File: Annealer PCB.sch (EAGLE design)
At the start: 36 parts

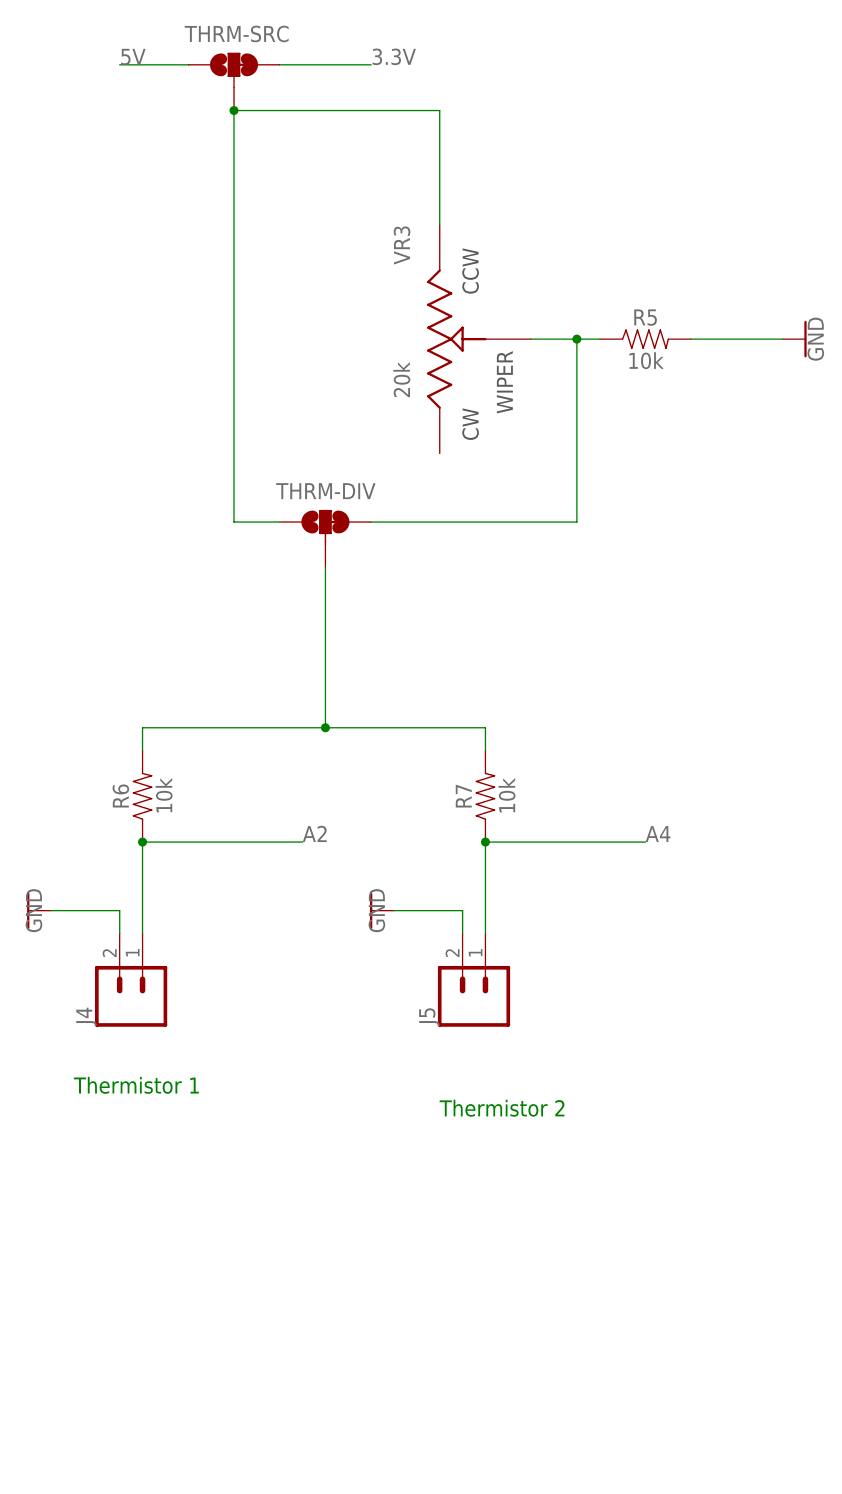
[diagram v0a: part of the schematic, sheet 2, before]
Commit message: v3.1 - source voltage for phototransistors
Source voltage was only 5v on v3.0. Changed design so that source voltage for thermistors AND phototransistors on the proximity sensors is fed by an appropriate reference voltage.
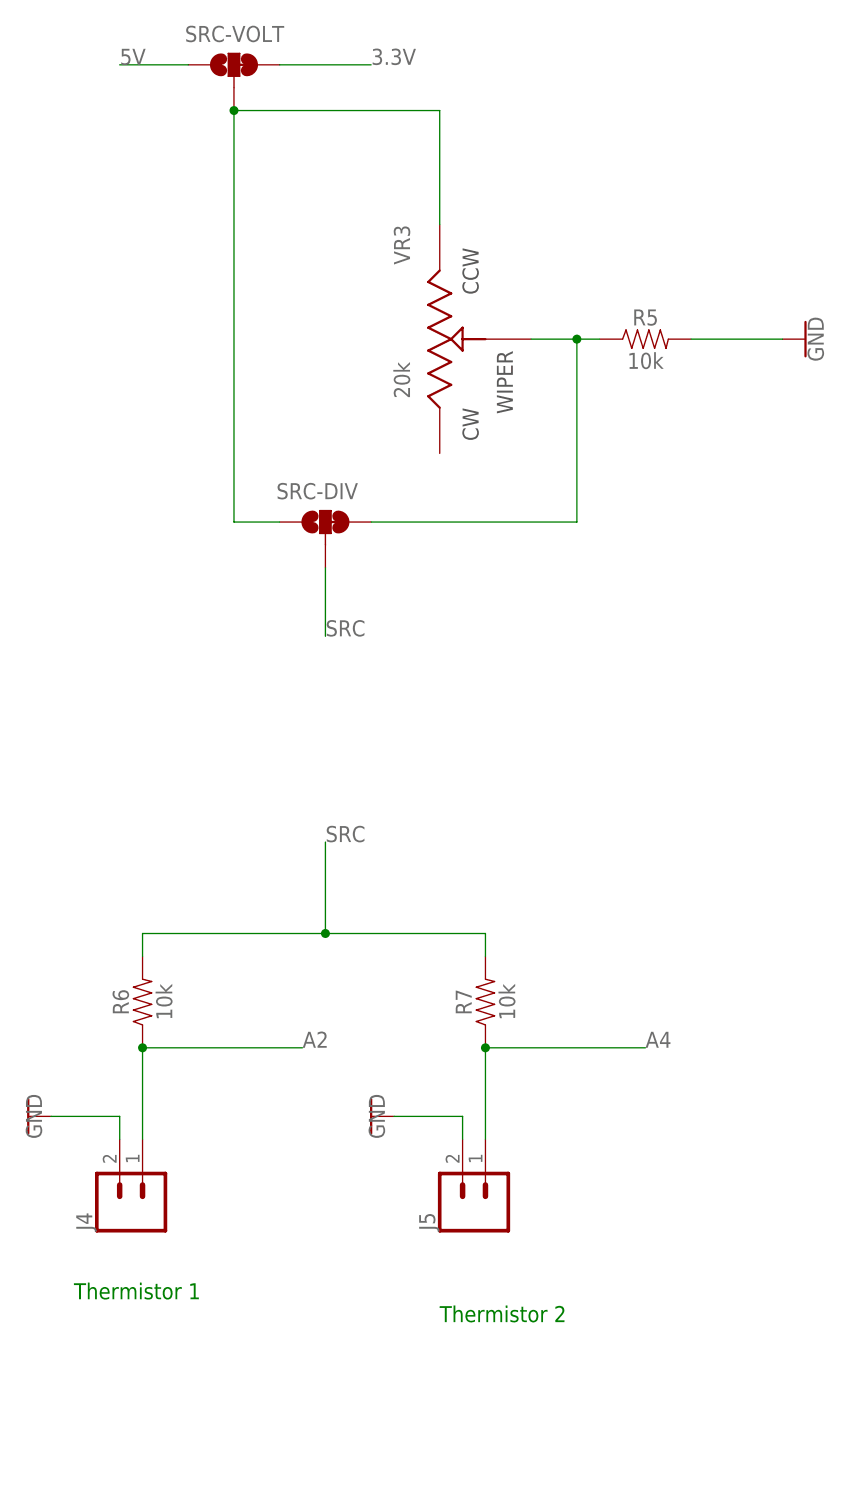
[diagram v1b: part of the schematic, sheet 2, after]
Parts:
- renumbered THRM-DIV to SRC-DIV, THRM-SRC to SRC-VOLT
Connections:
- removed net N$1: R6.2, R7.2, SRC-DIV.2
- new net SRC: R10.2, R4.2, R6.2, R7.2, SRC-DIV.2
- net 5V: no longer R10.2, R4.2
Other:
- note added: "I2C"
- moved on the sheet: J4, J5, R6, R7

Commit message: v3.2 - source voltage for proximity detectors
Changed voltage handling for proximity sensors to avoid disrupting thermistor measurements when a phototransistor detects light inbound. Each phototransistor should have it's own input source and voltage divider. The thermistors share a common, separate input. Voltage dividers on each are bypassable.
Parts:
- removed SRC-VOLT: JUMPER-SMT_3_1-NC_TRACE_SILK, SparkFun-Jumpers:JUMPER-SMT_3_1-NC_TRACE_SILK
- added R12, R13: 10k, SparkFun-Resistors:10KOHM-HORIZ-1/4W-1%
- added R14, R15: 6800, SparkFun-Resistors:RESISTORAXIAL-0.3
- added REF-VOLT, T1-BYPASS, T2-BYPASS: JUMPER-SMT_3_1-NC_TRACE_SILK, SparkFun-Jumpers:JUMPER-SMT_3_1-NC_TRACE_SILK
- renumbered SRC-DIV to THERM-DIV
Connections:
- new net N$1: R4.2, T1-BYPASS.2
- new net N$11: R12.2, R14.2, T1-BYPASS.3
- new net N$13: R13.2, R15.2, T2-BYPASS.3
- new net VREF: R14.1, R15.1, REF-VOLT.2, T1-BYPASS.1, T2-BYPASS.1, THERM-DIV.1, VR3.1
- net 3.3V: now also REF-VOLT.3; no longer SRC-VOLT.3
- net 5V: now also REF-VOLT.1; no longer SRC-VOLT.1
- net GND: now also R12.1, R13.1
- net N$8: now also R10.2, T2-BYPASS.2; no longer SRC-VOLT.2, THERM-DIV.1, VR3.1
- net SRC: no longer R10.2, R4.2
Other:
- moved on the sheet: J10, J3, R10, R11, R3, R4

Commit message: v4 board update
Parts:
- removed R10, R12, R13, R4: 10k, SparkFun-Resistors:10KOHM-HORIZ-1/4W-1%
- removed R11, R3: 330, SparkFun-Resistors:330OHM-HORIZ-1/10W-5%
- removed R14, R15: 6800, SparkFun-Resistors:RESISTORAXIAL-0.3
- removed T1-BYPASS, T2-BYPASS: JUMPER-SMT_3_1-NC_TRACE_SILK, SparkFun-Jumpers:JUMPER-SMT_3_1-NC_TRACE_SILK
- J10, J3: value (none) -> CONN_5X1_MOLEX_POLAR; device SparkFun-Connectors:CONN_04POLAR -> dave-connectors:CONN_5X1_MOLEX_POLAR
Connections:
- removed net N$1: R4.2, T1-BYPASS.2
- removed net N$11: R12.2, R14.2, T1-BYPASS.3
- removed net N$13: R13.2, R15.2, T2-BYPASS.3
- removed net N$15: J3.3, R3.1
- removed net N$6: J10.3, R11.1
- removed net N$8: R10.2, T2-BYPASS.2
- net 5V: now also J10.4, J3.4; no longer R11.2, R3.2
- net A3: no longer R4.1
- net A5: no longer R10.1
- net D2: now also J8.3; no longer J9.1
- net D3: now also J8.1; no longer J11.1
- net D6: now also J9.1; no longer J8.1
- net D7: now also J11.1; no longer J8.3
- net GND: now also J10.3, J10.5, J3.3, J3.5; no longer J10.2, J10.4, J3.2, J3.4, R12.1, R13.1
- net VREF: now also J10.2, J3.2; no longer R14.1, R15.1, T1-BYPASS.1, T2-BYPASS.1

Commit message: 4.1 - add power-on LED
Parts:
- added J14: (no value), SparkFun-Connectors:CONN_02POLAR
- added R3: 330, SparkFun-Resistors:330OHM-HORIZ-1/10W-5%
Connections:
- new net N$1: J14.1, R3.1
- net 5V: now also R3.2
- net GND: now also J14.2
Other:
- note added: "Power LED"
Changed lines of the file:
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@@
 <part name="J10" library="dave-connectors" deviceset="CONN_5X1_MOLEX_POLAR" device=""/>
 <part name="GND6" library="SparkFun-PowerSymbols" deviceset="GND" device=""/>
+<part name="J14" library="SparkFun-Connectors" deviceset="CONN_02" device="POLAR"/>
+<part name="R3" library="SparkFun-Resistors" deviceset="330OHM" device="-HORIZ-1/10W-5%" value="330"/>
+<part name="GND16" library="SparkFun-PowerSymbols" deviceset="GND" device=""/>
 </parts>
 <sheets>
@@
 <text x="180.34" y="0" size="1.778" layer="91">Proximity Sensor 2</text>
 <text x="-53.34" y="-15.24" size="1.778" layer="91">I2C</text>
+<text x="129.54" y="66.04" size="1.778" layer="91">Power LED</text>
 </plain>
 <instances>
@@
 <instance part="GND6" gate="1" x="154.94" y="48.26" smashed="yes" rot="R90">
 <attribute name="VALUE" x="155.194" y="48.26" size="1.778" layer="96" rot="R270" align="top-center"/>
+</instance>
+<instance part="J14" gate="G$1" x="137.16" y="73.66" smashed="yes" rot="R90">
+<attribute name="VALUE" x="141.986" y="71.12" size="1.778" layer="96" font="vector" rot="R90"/>
+<attribute name="NAME" x="131.572" y="71.12" size="1.778" layer="95" font="vector" rot="R90"/>
+</instance>
+<instance part="R3" gate="G$1" x="137.16" y="99.06" smashed="yes" rot="R90">
+<attribute name="NAME" x="135.636" y="99.06" size="1.778" layer="95" font="vector" rot="R90" align="bottom-center"/>
+<attribute name="VALUE" x="138.684" y="99.06" size="1.778" layer="96" font="vector" rot="R90" align="top-center"/>
+</instance>
+<instance part="GND16" gate="1" x="127" y="88.9" smashed="yes" rot="R270">
+<attribute name="VALUE" x="126.746" y="88.9" size="1.778" layer="96" rot="R90" align="top-center"/>
 </instance>
 </instances>
@@
 <junction x="200.66" y="38.1"/>
 </segment>
+<segment>
+<pinref part="J14" gate="G$1" pin="2"/>
+<wire x1="134.62" y1="81.28" x2="134.62" y2="88.9" width="0.1524" layer="91"/>
+<pinref part="GND16" gate="1" pin="GND"/>
+<wire x1="134.62" y1="88.9" x2="129.54" y2="88.9" width="0.1524" layer="91"/>
+</segment>
 </net>
 <net name="3.3V" class="0">
@@
 <wire x1="195.58" y1="27.94" x2="195.58" y2="43.18" width="0.1524" layer="91"/>
 <label x="195.58" y="43.18" size="1.778" layer="95"/>
+</segment>
+<segment>
+<pinref part="R3" gate="G$1" pin="2"/>
+<wire x1="137.16" y1="104.14" x2="137.16" y2="111.76" width="0.1524" layer="91"/>
+<label x="137.16" y="111.76" size="1.778" layer="95"/>
 </segment>
 </net>
@@
 </segment>
 </net>
+<net name="N$1" class="0">
+<segment>
+<pinref part="R3" gate="G$1" pin="1"/>
+<pinref part="J14" gate="G$1" pin="1"/>
+<wire x1="137.16" y1="93.98" x2="137.16" y2="81.28" width="0.1524" layer="91"/>
+</segment>
+</net>
